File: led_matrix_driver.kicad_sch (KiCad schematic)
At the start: 18 parts, among them J2 Screw_Terminal_01x02, J3 Screw_Terminal_01x02, J4 Conn_01x06_Pin, J5 Conn_02x17_Odd_Even, SW2 CK_KMS2xxGP, U2 Pico, U3 ESP32-WROOM-32, U4 AP1117-33, U6 Teensy4.0, U7 74AHCT541, U8 74AHCT541

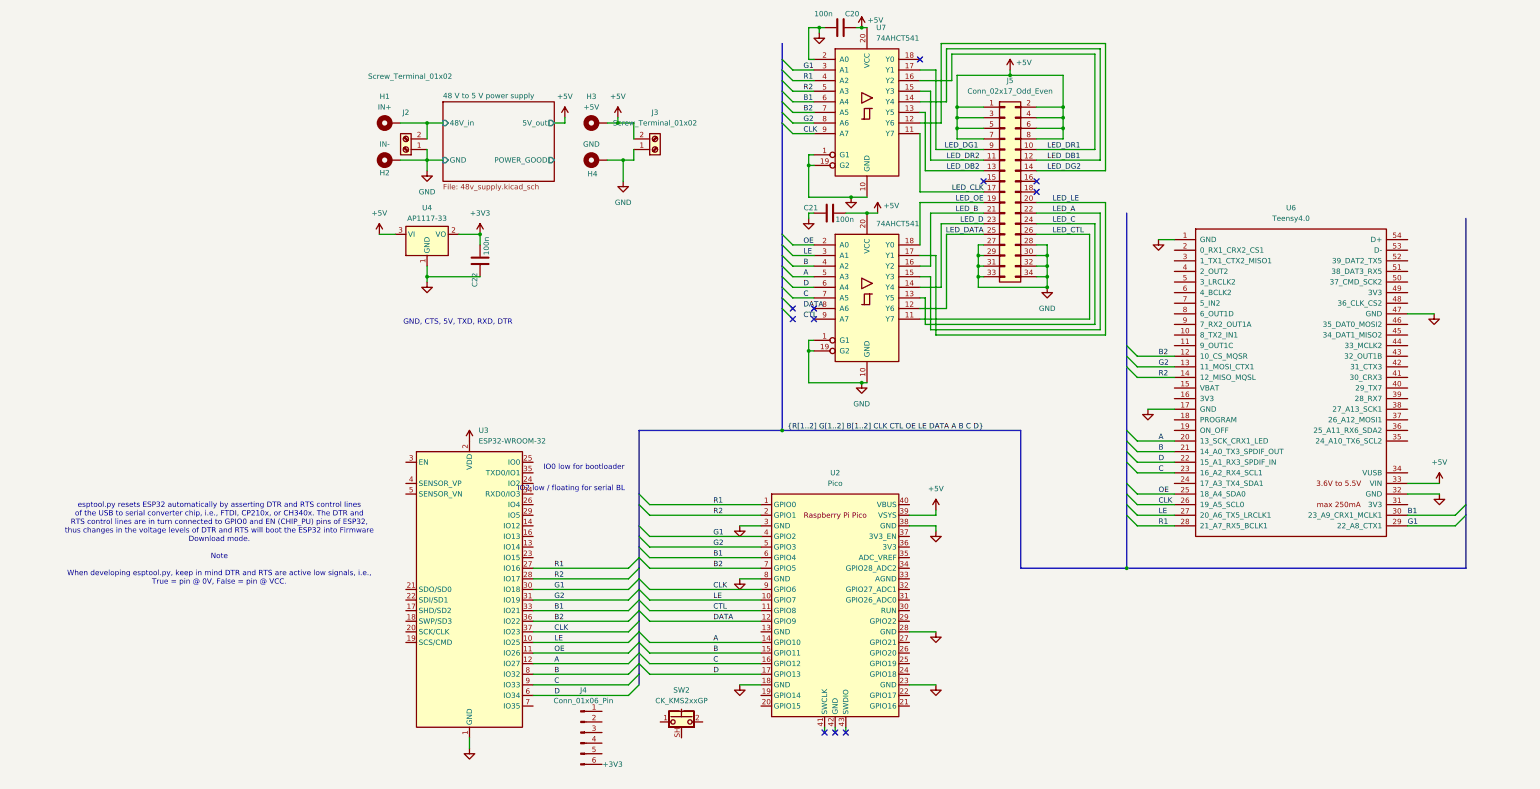
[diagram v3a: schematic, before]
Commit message: Fixed ERC indicated issues. Added ESP32 programming connection.
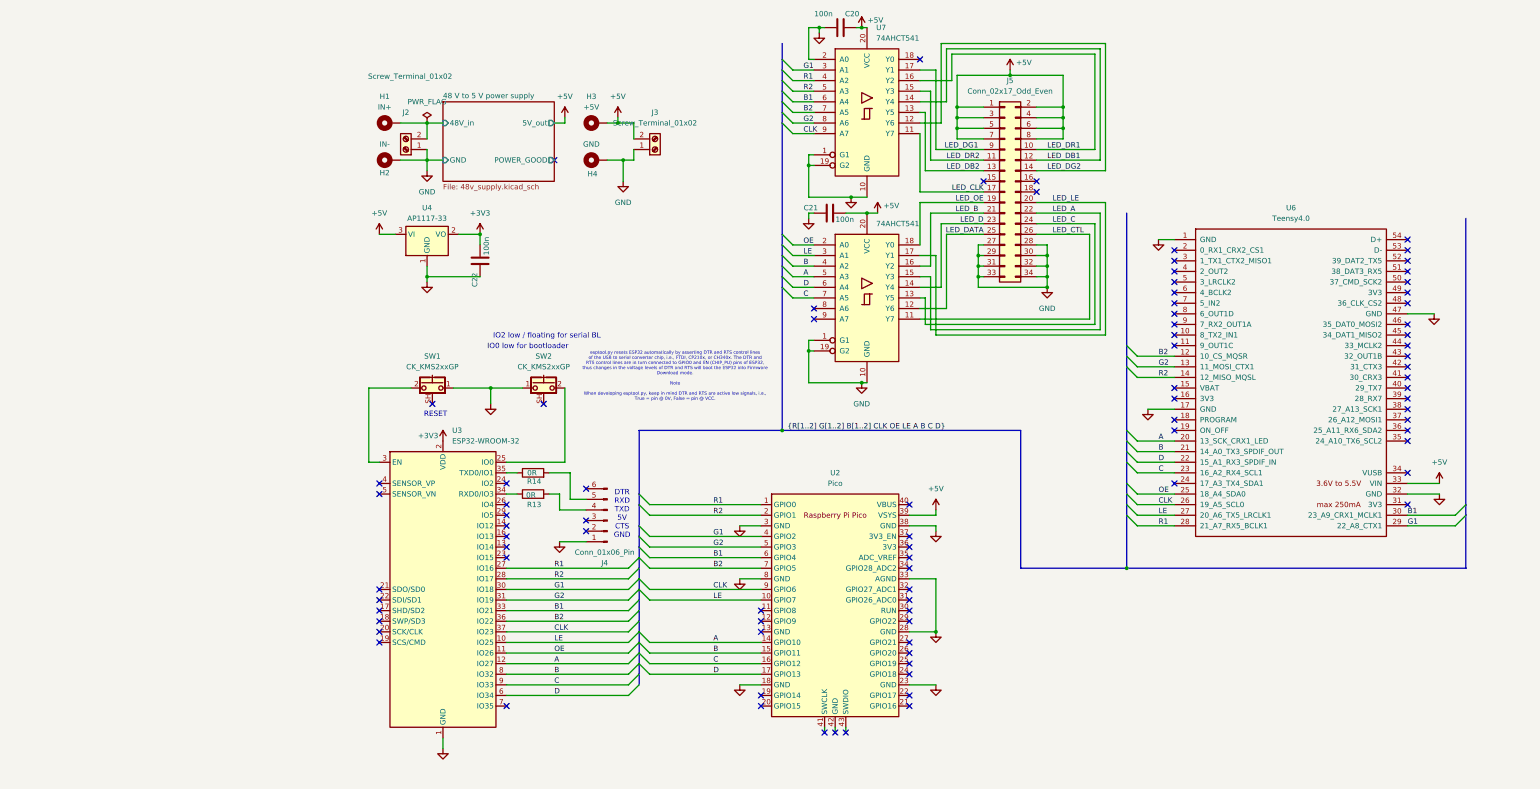
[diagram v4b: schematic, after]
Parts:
- added R13, R14: 0R, Resistor_SMD:R_0603_1608Metric, symbol Device:R
- added SW1: CK_KMS2xxGP, Button_Switch_SMD:SW_SPST_CK_KMS2xxGP, symbol Switch:CK_KMS2xxGP
- U2: footprint MCU_RaspberryPi_and_Boards:RPi_Pico_SMD_TH -> RPi_Pico:RPi_Pico_SMD_TH
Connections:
- net GND: now also J4.1 (Pin_1), SW2.1, U2.33 (AGND), SW1.1
- net at SW2.2: now also U3.25 (IO0)
- net at U3.3 (EN): now also SW1.2
- net at U3.34 (RXD0/IO3): now also R13.1
- net at U3.35 (TXD0/IO1): now also R14.1
- net at J4.4 (Pin_4): now also R13.2
- net at J4.5 (Pin_5): now also R14.2
- net CTL: no longer names the net of U2.11 (GPIO8)
- net DATA: no longer names the net of U2.12 (GPIO9)
- no-connect marks 11 -> 87
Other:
- note added: "DTR RXD TXD 5V CTS GND"
- note added: "RESET"
- note removed: "GND, CTS, 5V, TXD, RXD, DTR"
- moved on the sheet: J4, SW2, U3

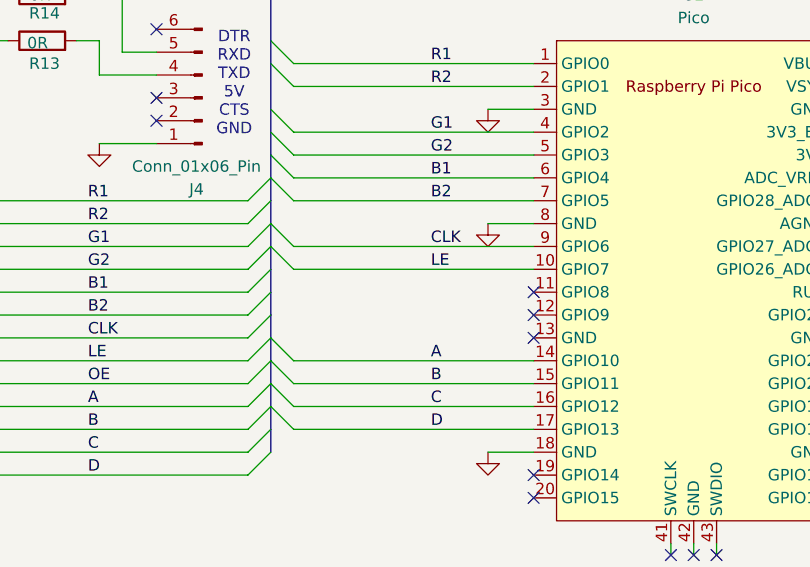
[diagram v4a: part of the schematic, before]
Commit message: Updated packages. Added OE to RPi Pico
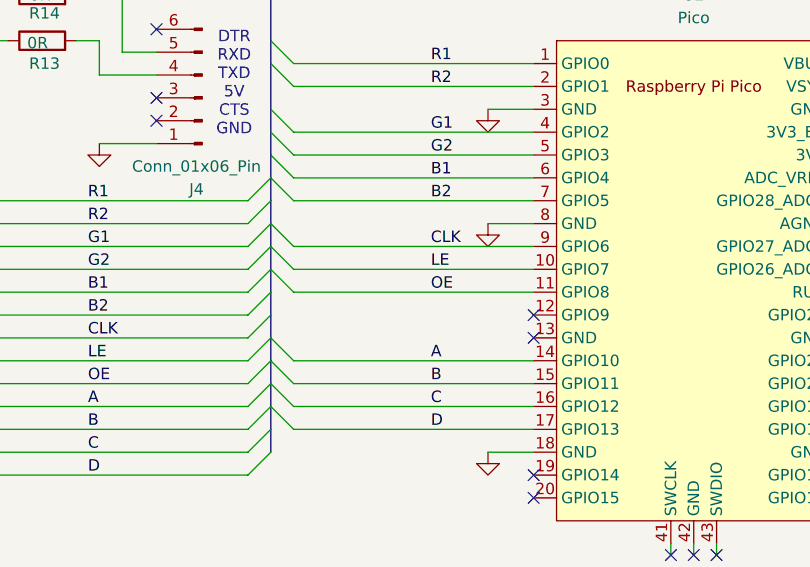
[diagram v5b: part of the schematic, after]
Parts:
- U2: footprint RPi_Pico:RPi_Pico_SMD_TH -> MCU_RaspberryPi_and_Boards:RPi_Pico_SMD_TH
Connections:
- net OE: now also U2.11 (GPIO8)
- no-connect marks 87 -> 86
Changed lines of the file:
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@@
 	)
 	(no_connect
-		(at 109.22 156.21)
-	)
-	(no_connect
 		(at 17.78 151.13)
 	)
@@
 	)
 	(bus_entry
+		(at 80.01 153.67)
+		(size 2.54 2.54)
+		(stroke
+			(width 0)
+			(type default)
+		)
+	)
+	(bus_entry
 		(at 114.3 66.04)
 		(size 2.54 2.54)
@@
 	(wire
 		(pts
+			(xy 82.55 156.21) (xy 109.22 156.21)
+		)
+		(stroke
+			(width 0)
+			(type default)
+		)
+	)
+	(wire
+		(pts
 			(xy 161.29 73.66) (xy 162.56 73.66)
 		)
@@
 		)
 	)
+	(label "OE"
+		(at 97.79 156.21 0)
+		(effects
+			(font
+				(size 1.27 1.27)
+			)
+			(justify left bottom)
+		)
+	)
 	(label "C"
 		(at 204.47 123.19 0)
@@
 			)
 		)
-		(property "Footprint" "RPi_Pico:RPi_Pico_SMD_TH"
+		(property "Footprint" "MCU_RaspberryPi_and_Boards:RPi_Pico_SMD_TH"
 			(at 127 154.94 90)
 			(effects

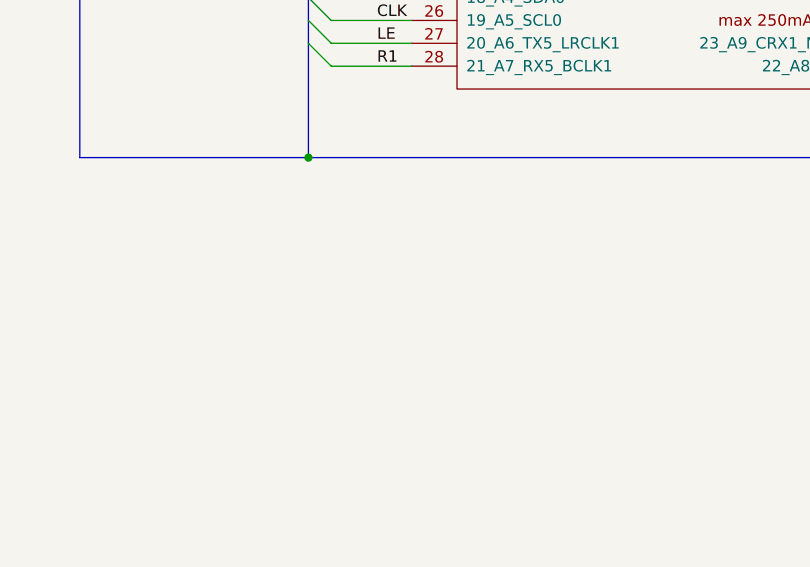
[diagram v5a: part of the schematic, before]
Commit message: Some mounting holes. Release to prod
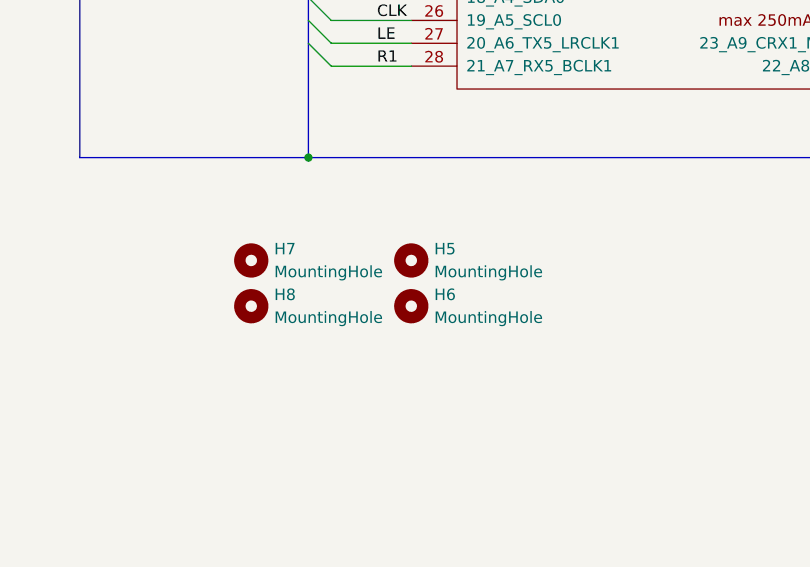
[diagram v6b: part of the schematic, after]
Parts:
- added H5, H6, H7, H8: MountingHole, MountingHole:MountingHole_3.2mm_M3, symbol Mechanical:MountingHole

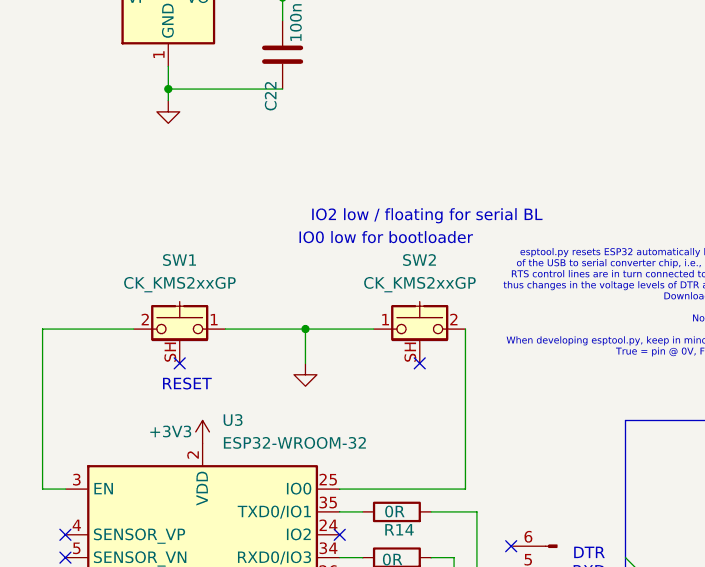
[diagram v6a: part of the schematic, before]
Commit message: Added DK order numbers
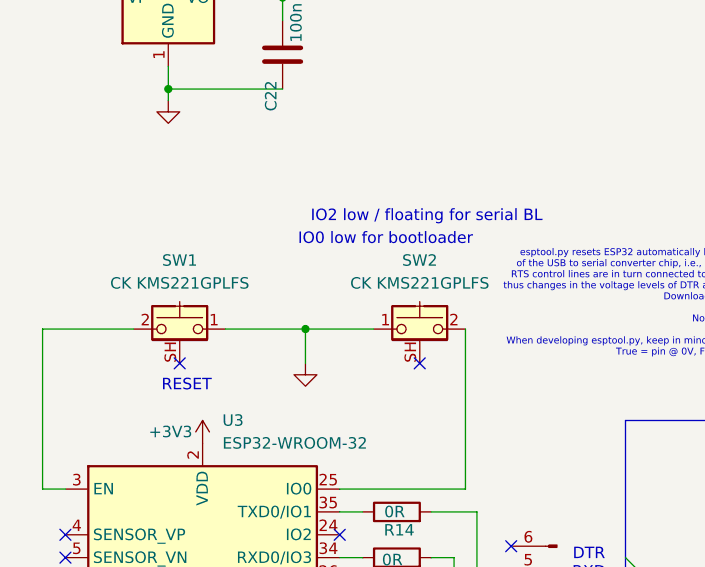
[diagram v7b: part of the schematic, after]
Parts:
- C20, C21, C22: DK (none) -> 1276-1006-1-ND
- H1, H2, H3, H4, H5, H6, H7, H8, J2, J3, J4, J5: DK (none) -> -
- R13, R14: DK (none) -> 541-0.0GCT-ND
- SW1, SW2: value CK_KMS2xxGP -> CK KMS221GPLFS; DK (none) -> 401-1614-1-ND
- U2: DK (none) -> 2648-SC0917-ND
- U3: DK (none) -> 5407-ESP32-WROOM-32E-N16CT-ND
- U4: DK (none) -> AZ1117CH-3.3TRG1DICT-ND
- U6: DK (none) -> 1568-DEV-15583-ND
- U7, U8: DK (none) -> 296-4754-1-ND
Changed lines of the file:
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@@
 	(label "OE"
 		(at 97.79 156.21 0)
+		(fields_autoplaced yes)
 		(effects
 			(font
@@
 			)
 		)
+		(property "DK" "-"
+			(at 20.32 48.26 0)
+			(effects
+				(font
+					(size 1.27 1.27)
+				)
+				(hide yes)
+			)
+		)
 		(pin "1"
 		)
@@
 			)
 		)
-		(property "Value" "CK_KMS2xxGP"
+		(property "Value" "CK KMS221GPLFS"
 			(at 30.48 97.79 0)
 			(effects
@@
 			)
 		)
+		(property "DK" "401-1614-1-ND"
+			(at 30.48 102.87 0)
+			(effects
+				(font
+					(size 1.27 1.27)
+				)
+				(hide yes)
+			)
+		)
 		(pin "1"
 		)
@@
 			)
 		)
+		(property "DK" "-"
+			(at 69.85 48.26 0)
+			(effects
+				(font
+					(size 1.27 1.27)
+				)
+				(hide yes)
+			)
+		)
 		(pin "1"
 		)
@@
 			)
 		)
+		(property "DK" "-"
+			(at 20.32 39.37 0)
+			(effects
+				(font
+					(size 1.27 1.27)
+				)
+				(hide yes)
+			)
+		)
 		(pin "1"
 		)
@@
 			)
 		)
+		(property "DK" "296-4754-1-ND"
+			(at 134.62 81.28 0)
+			(effects
+				(font
+					(size 1.27 1.27)
+				)
+				(hide yes)
+			)
+		)
 		(pin "13"
 		)
@@
 			)
 		)
+		(property "DK" "-"
+			(at 69.85 39.37 0)
+			(effects
+				(font
+					(size 1.27 1.27)
+				)
+				(hide yes)
+			)
+		)
 		(pin "1"
 		)
@@
 			)
 		)
+		(property "DK" "AZ1117CH-3.3TRG1DICT-ND"
+			(at 29.21 66.04 0)
+			(effects
+				(font
+					(size 1.27 1.27)
+				)
+				(hide yes)
+			)
+		)
 		(pin "2"
 		)
@@
 			)
 		)
-		(property "Value" "CK_KMS2xxGP"
+		(property "Value" "CK KMS221GPLFS"
 			(at 57.15 97.79 0)
 			(effects
@@
 			)
 		)
+		(property "DK" "401-1614-1-ND"
+			(at 57.15 102.87 0)
+			(effects
+				(font
+					(size 1.27 1.27)
+				)
+				(hide yes)
+			)
+		)
 		(pin "1"
 		)
@@
 			)
 		)
+		(property "DK" "-"
+			(at 24.13 45.72 0)
+			(effects
+				(font
+					(size 1.27 1.27)
+				)
+				(hide yes)
+			)
+		)
 		(pin "1"
 		)
@@
 			)
 		)
+		(property "DK" "-"
+			(at 167.64 55.88 0)
+			(effects
+				(font
+					(size 1.27 1.27)
+				)
+				(hide yes)
+			)
+		)
 		(pin "10"
 		)
@@
 			)
 		)
+		(property "DK" "-"
+			(at 83.82 45.72 0)
+			(effects
+				(font
+					(size 1.27 1.27)
+				)
+				(hide yes)
+			)
+		)
 		(pin "1"
 		)
@@
 			)
 		)
+		(property "DK" "2648-SC0917-ND"
+			(at 127 154.94 0)
+			(effects
+				(font
+					(size 1.27 1.27)
+				)
+				(hide yes)
+			)
+		)
 		(pin "17"
 		)
@@
 			)
 		)
+		(property "DK" "-"
+			(at 208.28 162.56 0)
+			(effects
+				(font
+					(size 1.27 1.27)
+				)
+				(hide yes)
+			)
+		)
 		(instances
 			(project "led_matrix_driver"
@@
 			)
 		)
+		(property "DK" "1276-1006-1-ND"
+			(at 128.27 16.51 0)
+			(effects
+				(font
+					(size 1.27 1.27)
+				)
+				(hide yes)
+			)
+		)
 		(pin "1"
 		)
@@
 			)
 		)
+		(property "DK" "1276-1006-1-ND"
+			(at 125.73 60.96 0)
+			(effects
+				(font
+					(size 1.27 1.27)
+				)
+				(hide yes)
+			)
+		)
 		(pin "1"
 		)
@@
 			)
 		)
+		(property "DK" "541-0.0GCT-ND"
+			(at 54.61 123.19 0)
+			(effects
+				(font
+					(size 1.27 1.27)
+				)
+				(hide yes)
+			)
+		)
 		(pin "2"
 		)
@@
 			)
 		)
+		(property "DK" "1276-1006-1-ND"
+			(at 41.91 72.39 0)
+			(effects
+				(font
+					(size 1.27 1.27)
+				)
+				(hide yes)
+			)
+		)
 		(pin "1"
 		)
@@
 			)
 		)
+		(property "DK" "296-4754-1-ND"
+			(at 134.62 36.83 0)
+			(effects
+				(font
+					(size 1.27 1.27)
+				)
+				(hide yes)
+			)
+		)
 		(pin "13"
 		)
@@
 			)
 		)
+		(property "DK" "-"
+			(at 208.28 157.48 0)
+			(effects
+				(font
+					(size 1.27 1.27)
+				)
+				(hide yes)
+			)
+		)
 		(instances
 			(project ""
@@
 			)
 		)
+		(property "DK" "5407-ESP32-WROOM-32E-N16CT-ND"
+			(at 33.02 151.13 0)
+			(effects
+				(font
+					(size 1.27 1.27)
+				)
+				(hide yes)
+			)
+		)
 		(pin "4"
 		)
@@
 			)
 		)
+		(property "DK" "541-0.0GCT-ND"
+			(at 54.61 128.27 0)
+			(effects
+				(font
+					(size 1.27 1.27)
+				)
+				(hide yes)
+			)
+		)
 		(pin "2"
 		)
@@
 			)
 		)
+		(property "DK" "-"
+			(at 190.5 162.56 0)
+			(effects
+				(font
+					(size 1.27 1.27)
+				)
+				(hide yes)
+			)
+		)
 		(instances
 			(project "led_matrix_driver"
@@
 			)
 		)
+		(property "DK" "1568-DEV-15583-ND"
+			(at 236.22 101.6 0)
+			(effects
+				(font
+					(size 1.27 1.27)
+				)
+				(hide yes)
+			)
+		)
 		(pin "10"
 		)
@@
 			)
 		)
+		(property "DK" "-"
+			(at 72.39 134.62 0)
+			(effects
+				(font
+					(size 1.27 1.27)
+				)
+				(hide yes)
+			)
+		)
 		(pin "2"
 		)
@@
 			(at 190.5 157.48 0)
 			(effects
+				(font
+					(size 1.27 1.27)
+				)
+				(hide yes)
+			)
+		)
+		(property "DK" "-"
+			(at 190.5 157.48 0)
+			(effects
